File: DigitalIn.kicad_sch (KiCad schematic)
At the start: 3 parts, among them U26 ADuM1200AR

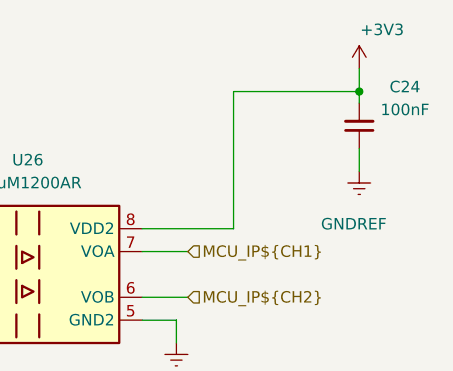
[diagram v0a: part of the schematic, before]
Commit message: Deleted stale test production files. Fixed up a bug with power isolation. Created some footprints for wire to board connectors although ran out of time to fix a bug where they do no lock in. Fixes to readme
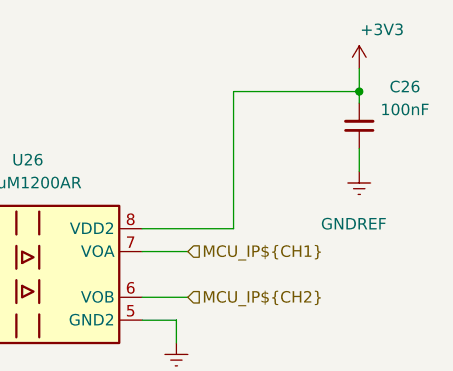
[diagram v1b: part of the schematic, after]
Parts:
- renumbered C24 to C26

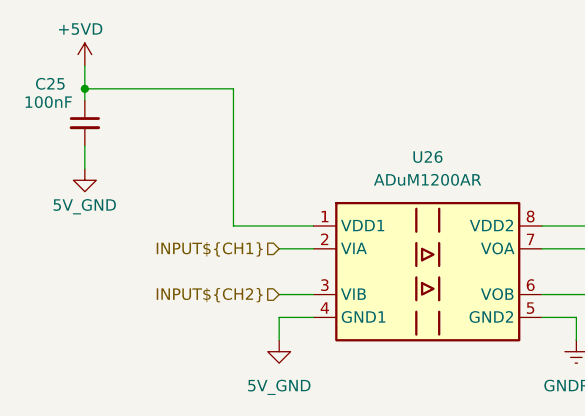
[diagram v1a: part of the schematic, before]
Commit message: restructured power supplies to enable Spindle DAC to be isolated. We now have the option of supplying two 24V inputs, one to power the nucleo and everything logic side and the other to power peripherals. Some testing will be required.
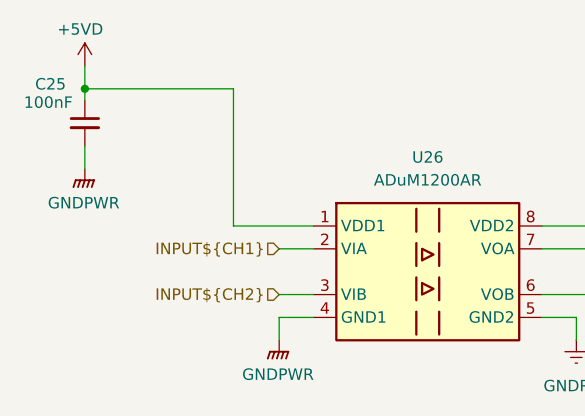
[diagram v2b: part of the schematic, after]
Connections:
- net 5V_GND renamed GNDPWR

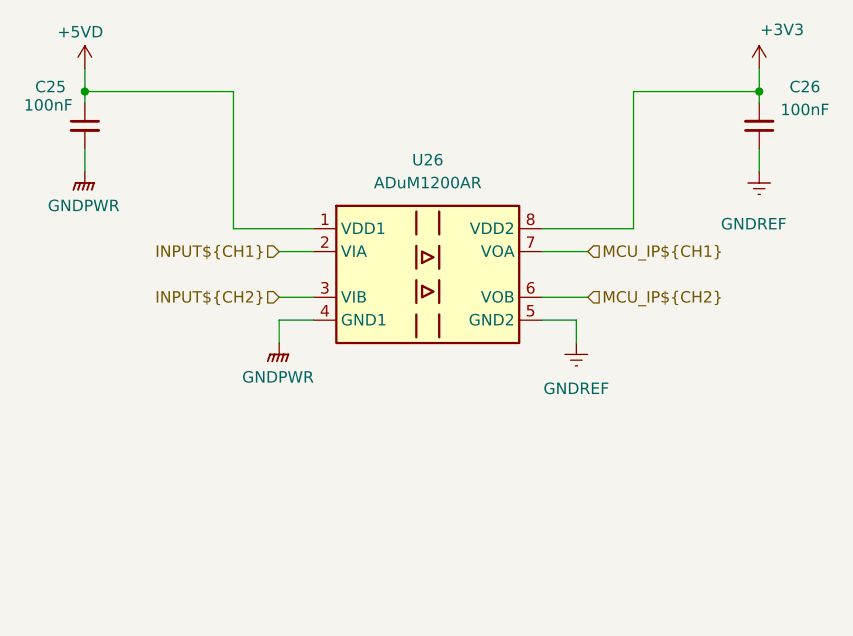
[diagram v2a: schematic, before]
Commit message: updates to read me, marked V1 parts inactive and made start on board layout for initial test board. fixes to BOM to suit
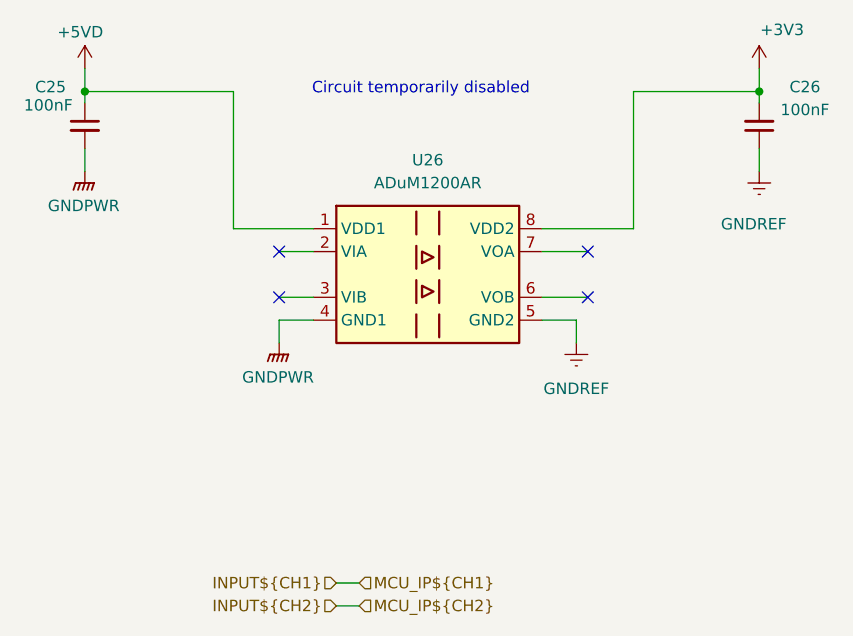
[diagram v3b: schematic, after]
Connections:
- net INPUT${CH1}: no longer U26.2 (VIA)
- net INPUT${CH2}: no longer U26.3 (VIB)
- net MCU_IP${CH1}: no longer names the net of U26.7 (VOA)
- net MCU_IP${CH2}: no longer names the net of U26.6 (VOB)
- no-connect marks 0 -> 4
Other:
- note added: "Circuit temporarily disabled"
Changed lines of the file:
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@@
 	(generator_version "9.0")
 	(paper "A4")
+	(text "Circuit temporarily disabled\n"
+		(exclude_from_sim no)
+		(at 137.668 70.866 0)
+		(effects
+			(font
+				(size 1.27 1.27)
+			)
+		)
+	)
 	(junction
 		(at 100.33 71.12)
@@
 		(color 0 0 0 0)
 	)
+	(no_connect
+		(at 121.92 88.9)
+	)
+	(no_connect
+		(at 121.92 93.98)
+	)
+	(no_connect
+		(at 156.21 88.9)
+	)
+	(no_connect
+		(at 156.21 93.98)
+	)
 	(wire
 		(pts
@@
 	(wire
 		(pts
+			(xy 128.27 128.27) (xy 130.81 128.27)
+		)
+		(stroke
+			(width 0)
+			(type default)
+		)
+	)
+	(wire
+		(pts
 			(xy 161.29 71.12) (xy 175.26 71.12)
 		)
@@
 		(pts
 			(xy 100.33 71.12) (xy 100.33 72.39)
+		)
+		(stroke
+			(width 0)
+			(type default)
+		)
+	)
+	(wire
+		(pts
+			(xy 128.27 125.73) (xy 130.81 125.73)
 		)
 		(stroke
@@
 	(hierarchical_label "INPUT${CH1}"
 		(shape input)
-		(at 121.92 88.9 180)
+		(at 128.27 125.73 180)
 		(effects
 			(font
@@
 	(hierarchical_label "MCU_IP${CH1}"
 		(shape input)
-		(at 156.21 88.9 0)
+		(at 130.81 125.73 0)
 		(effects
 			(font
@@
 	(hierarchical_label "MCU_IP${CH2}"
 		(shape input)
-		(at 156.21 93.98 0)
+		(at 130.81 128.27 0)
 		(effects
 			(font
@@
 	(hierarchical_label "INPUT${CH2}"
 		(shape input)
-		(at 121.92 93.98 180)
+		(at 128.27 128.27 180)
 		(effects
 			(font
@@
 		(exclude_from_sim no)
 		(in_bom yes)
-		(on_board yes)
+		(on_board no)
 		(dnp no)
 		(property "Reference" "C25"
@@
 		(exclude_from_sim no)
 		(in_bom yes)
-		(on_board yes)
+		(on_board no)
 		(dnp no)
 		(property "Reference" "C26"
@@
 		(exclude_from_sim no)
 		(in_bom yes)
-		(on_board yes)
+		(on_board no)
 		(dnp no)
 		(fields_autoplaced yes)

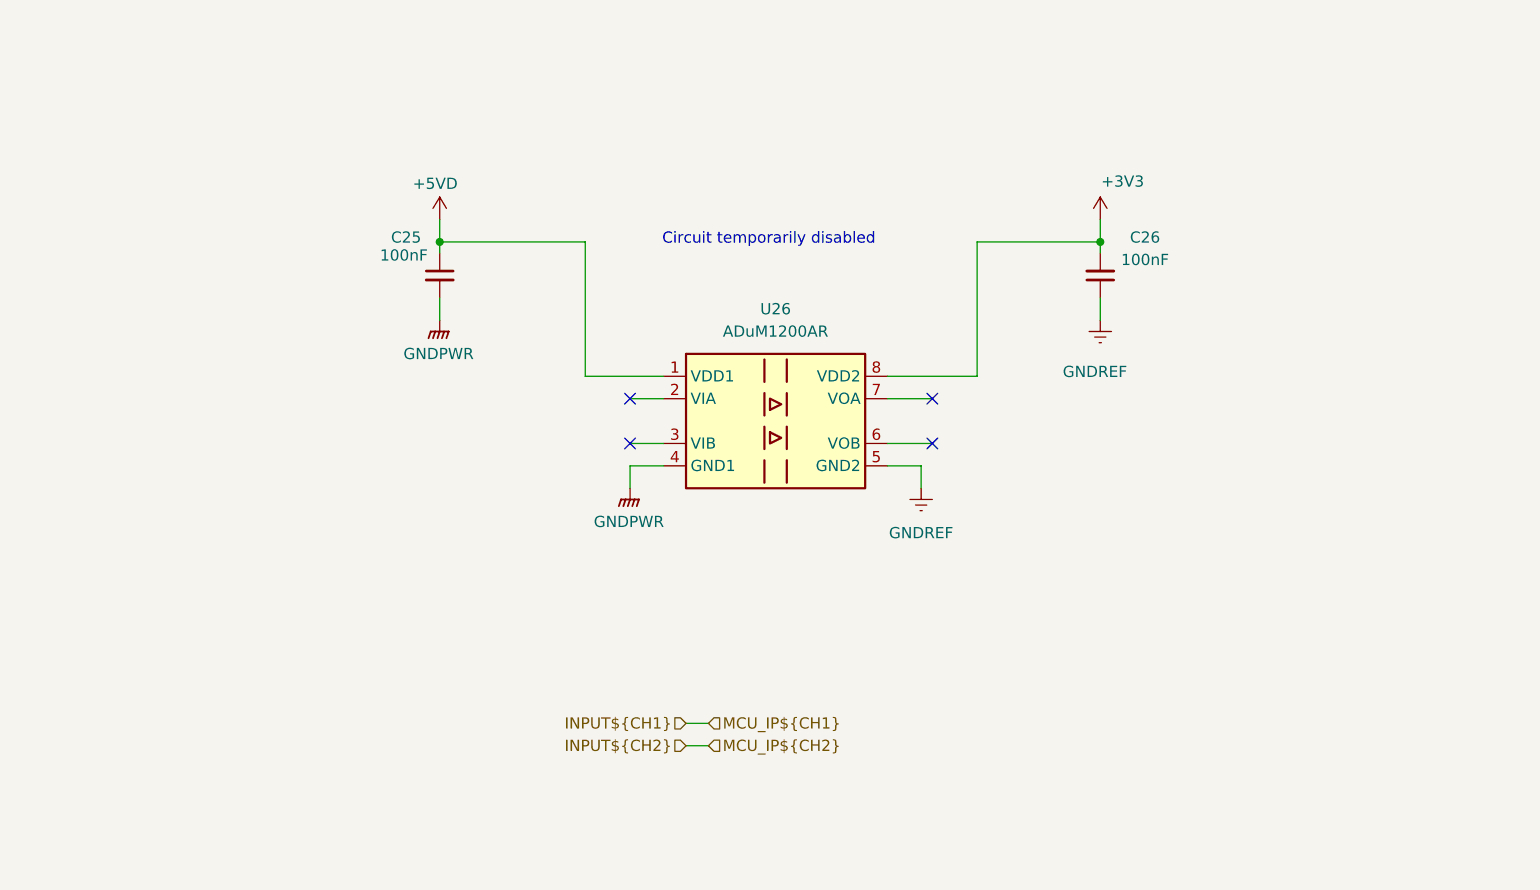
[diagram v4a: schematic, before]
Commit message: New optocoupler part choice, removed digikey BOM as have started inputting them into symbol fields. Re-enabled all disabled parts for now and will re-design power supplies soon.
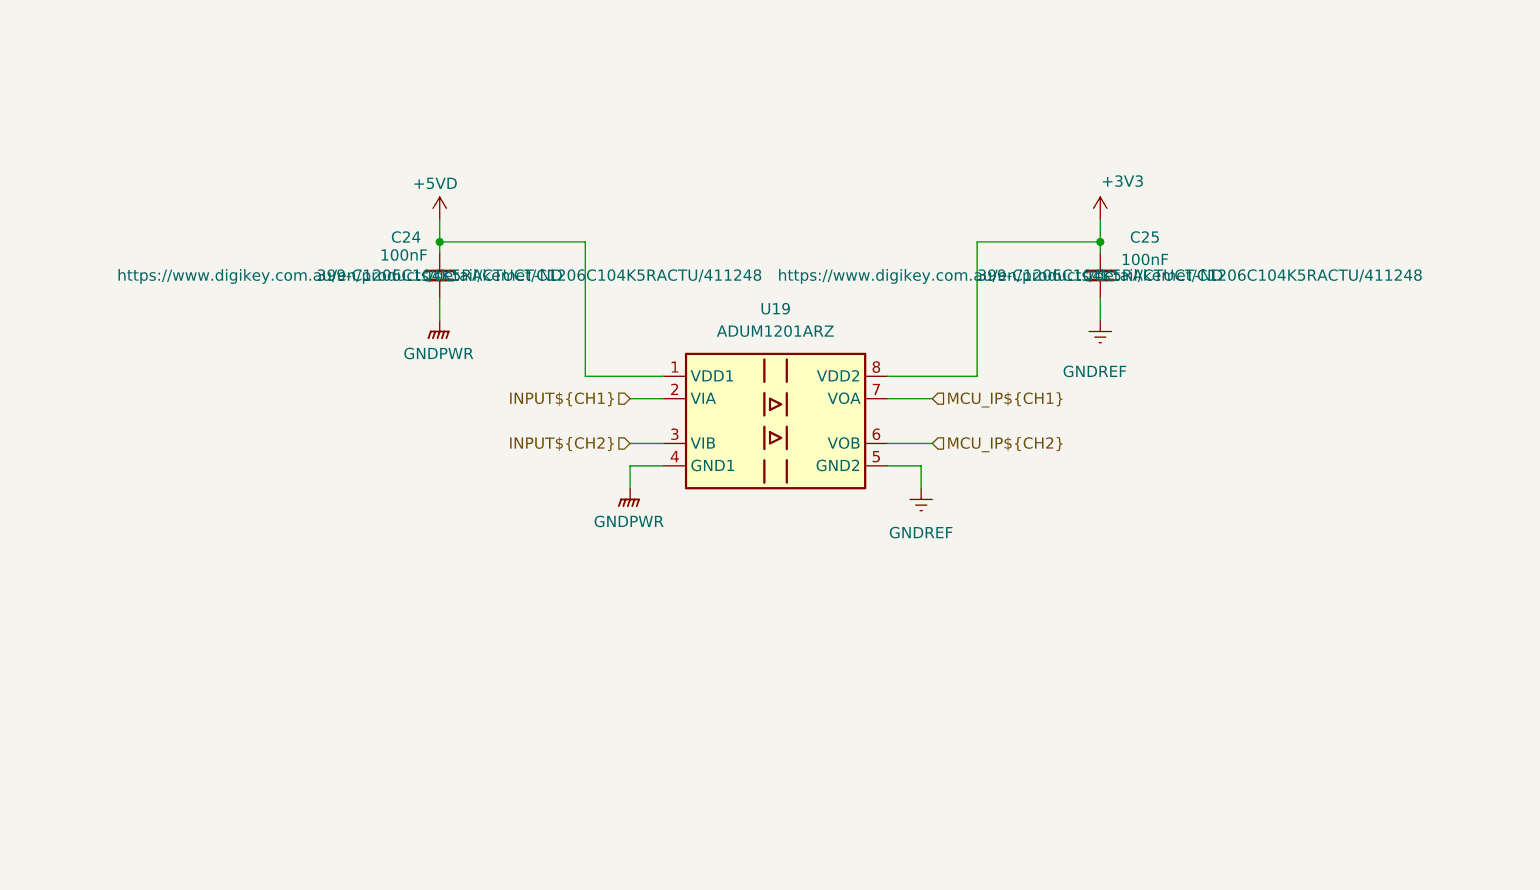
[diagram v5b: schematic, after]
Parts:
- C24: renamed from C25; Digikey Part Number (none) -> 399-C1206C104K5RACTUCT-ND; Digikey URL (none) -> https://www.digikey.com.au/en/products/detail/kemet/C1206C1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
- C25: renamed from C26; Digikey Part Number (none) -> 399-C1206C104K5RACTUCT-ND; Digikey URL (none) -> https://www.digikey.com.au/en/products/detail/kemet/C1206C1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
- U19: renamed from U26; value ADuM1200AR -> ADUM1201ARZ
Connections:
- net INPUT${CH1}: now also U19.2 (VIA)
- net INPUT${CH2}: now also U19.3 (VIB)
- net MCU_IP${CH2}: now reaches U19.6 (VOB)
- net MCU_IP${CH1}: now reaches U19.7 (VOA)
- no-connect marks 4 -> 0
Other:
- note removed: "Circuit temporarily disabled"

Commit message: fix to annoying additional symbol fields displaying when we didn't want them to.
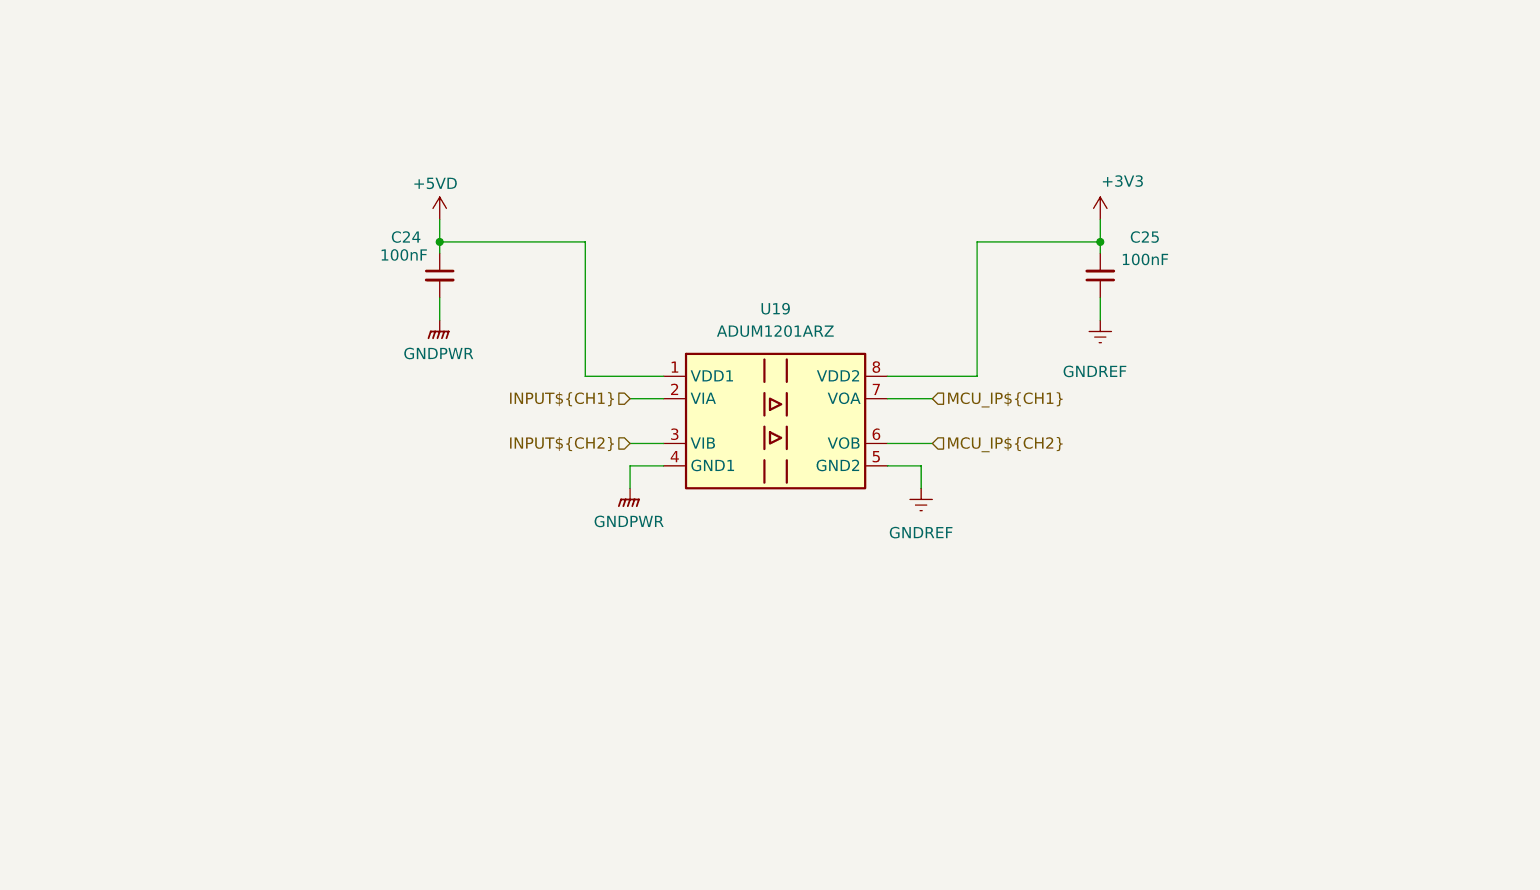
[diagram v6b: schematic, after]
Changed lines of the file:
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@@
 					(size 1.27 1.27)
 				)
+				(hide yes)
 			)
 		)
@@
 					(size 1.27 1.27)
 				)
+				(hide yes)
 			)
 		)
@@
 					(size 1.27 1.27)
 				)
+				(hide yes)
 			)
 		)
@@
 					(size 1.27 1.27)
 				)
+				(hide yes)
 			)
 		)
@@
 					(size 1.27 1.27)
 				)
+				(hide yes)
 			)
 		)
@@
 					(size 1.27 1.27)
 				)
-			)
-		)
+				(hide yes)
+			)
+		)

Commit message: BOM consolidation for various resistors. Moved BOM into symbol libraries and updated supplimentary BOM. Switched IO optical isolation circuitry to a more cost effective part.
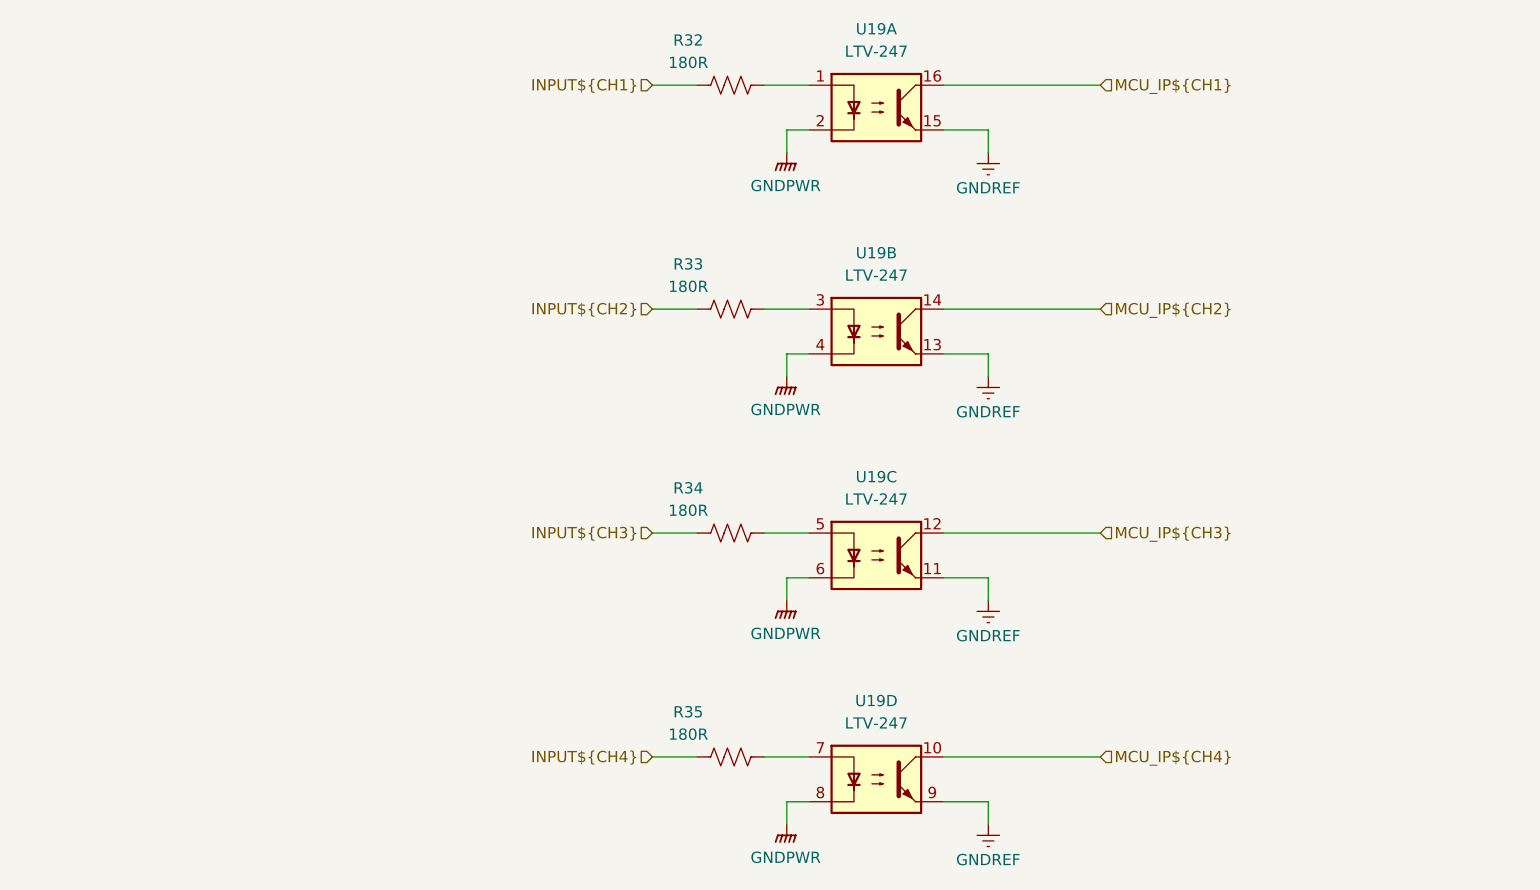
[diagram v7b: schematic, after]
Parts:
- removed C24, C25: 100nF, Capacitor_SMD:C_1206_3216Metric_Pad1.33x1.80mm_HandSolder, symbol Device:C_Small
- removed U19: ADUM1201ARZ, Package_SO:SOIC-8_3.9x4.9mm_P1.27mm, symbol Isolator:ADuM1200AR
- added R32, R33, R34, R35: 180R, Resistor_SMD:R_1206_3216Metric_Pad1.30x1.75mm_HandSolder, symbol Device:R_US
- added U19: LTV-247, Package_SO:SOP-16_4.4x10.4mm_P1.27mm, symbol Isolator:LTV-247
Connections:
- net GNDPWR: now also U19.2, U19.4, U19.6, U19.8
- net GNDREF: now also U19.11, U19.13, U19.15, U19.9
- net INPUT${CH1}: now also R32.1
- net INPUT${CH2}: now also R33.1
- net MCU_IP${CH1}: now also U19.16
- net MCU_IP${CH2}: now also U19.14
- new net: R35.2, U19.7
- new net: R32.2, U19.1
- new net: R33.2, U19.3
- new net: R34.2, U19.5
- new net INPUT${CH3}: R34.1
- new net INPUT${CH4}: R35.1
- new net MCU_IP${CH3}: U19.12
- new net MCU_IP${CH4}: U19.10

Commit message: New PSU designs + footprints assigned. Changes to board shape to make room for new components. BOM consolidation of supplimentary file
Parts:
- renumbered U19 to U7
